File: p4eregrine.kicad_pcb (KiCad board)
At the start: 6 copper layers, 39.5 x 39.5 mm, 359 parts, among them J5 Conn_Coaxial, Q10 NMOS, Q11 NMOS, Q12 NMOS, Q13 NMOS, Q14 NMOS, Q15 NMOS, Q16 NMOS, Q17 NMOS, Q18 NMOS, Q19 NMOS, Q20 NMOS, Q21 NMOS, Q22 NMOS, Q23 NMOS, Q24 NMOS, Q25 NMOS, Q26 NMOS, Q27 NMOS, Q28 NMOS, Q5 NMOS, Q6 NMOS, Q7 NMOS, Q8 NMOS, Q9 NMOS, U1 ESP32-P4NRW32X, U10 FPC-1.0FX-15PWCR-H20, U11 VL53L1CXV0FY1, U12 LIS2MDL, U13 LSM6DS3, U14 PMW3901MB-TXQT_C43496881, U15 TPD2EUSB30A, U16 DRV8328ARUYR, U17 TPS62933, U19 DRV8328ARUYR, U2 LPS22HB, U20 STM32G071GBU6, U22 DRV8328ARUYR, U23 STM32G071GBU6, U25 DRV8328ARUYR, U26 STM32G071GBU6, U3 W25Q128JVP, U30 STM32G071GBU6, U4 ESP32-C5HF4, U5 LFD182G45DCHD277, U6 TLV62569DBV, U7 GT-USB-7079C, U8 INA190A2IDCKR, U9 TPS2121RUXR, Y1 Crystal_GND24, Y2 Crystal_GND24

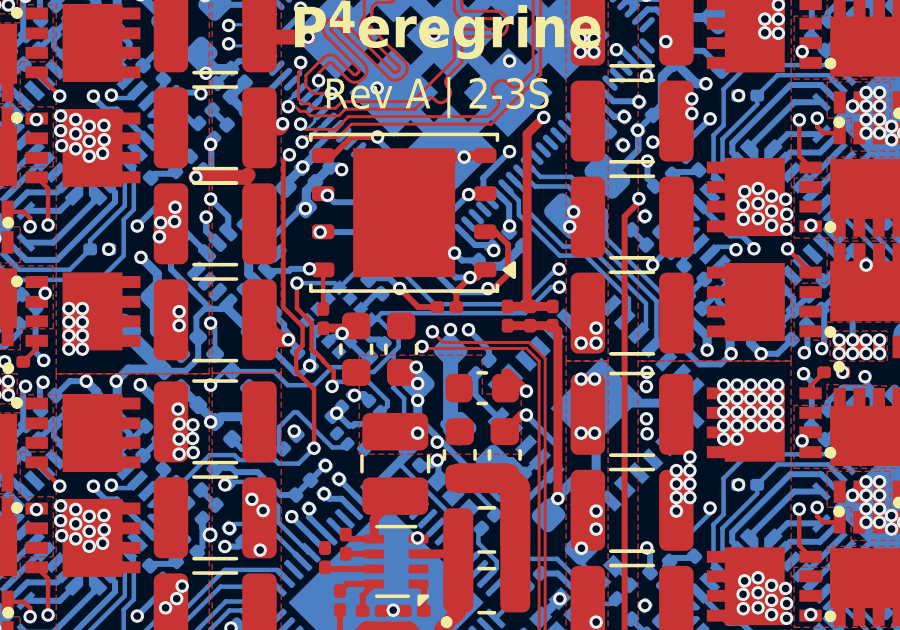
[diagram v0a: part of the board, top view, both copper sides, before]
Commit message: Add power supply comments to schematic
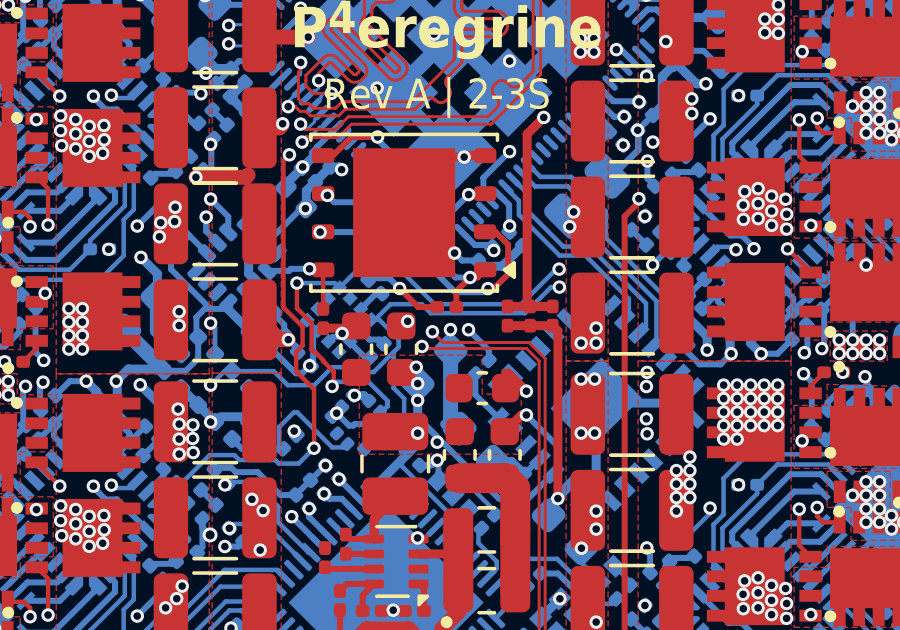
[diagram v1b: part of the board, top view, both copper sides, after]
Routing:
- net GND: vias 257 -> 258
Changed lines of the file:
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@@
 	)
 	(via
+		(at 149.512973 88.370643)
+		(size 0.45)
+		(drill 0.25)
+		(layers "F.Cu" "B.Cu")
+		(remove_unused_layers yes)
+		(keep_end_layers yes)
+		(free yes)
+		(zone_layer_connections "In1.Cu" "In4.Cu")
+		(net "GND")
+	)
+	(via
 		(at 145.535377 88.982263)
 		(size 0.45)
@@
 	)
 	(segment
+		(start 150.282378 88.1)
+		(end 149.982378 87.8)
+		(width 0.15)
+		(layer "B.Cu")
+		(net "I2C_SDA")
+	)
+	(segment
 		(start 145.046825 90.030702)
 		(end 145.516123 90.5)
@@
 	)
 	(segment
+		(start 154.571253 87.230505)
+		(end 154.293759 87.230505)
+		(width 0.15)
+		(layer "B.Cu")
+		(net "I2C_SDA")
+	)
+	(segment
 		(start 157.204961 81.035675)
 		(end 157.22458 81.055295)
@@
 	)
 	(segment
-		(start 147 89.9)
-		(end 147.953848 89.9)
+		(start 148.941206 87.8)
+		(end 148.425303 88.315903)
 		(width 0.15)
 		(layer "B.Cu")
@@
 	)
 	(segment
-		(start 153.424264 88.1)
-		(end 148.641206 88.1)
+		(start 147 89.9)
+		(end 147.953848 89.9)
 		(width 0.15)
 		(layer "B.Cu")
@@
 	)
 	(segment
-		(start 154.293759 87.230505)
-		(end 153.424264 88.1)
+		(start 148.560682 92.435816)
+		(end 149.056824 92.435816)
 		(width 0.15)
 		(layer "B.Cu")
@@
 	)
 	(segment
-		(start 148.560682 92.435816)
-		(end 149.056824 92.435816)
+		(start 148.425303 88.315903)
+		(end 148.301788 88.315903)
 		(width 0.15)
 		(layer "B.Cu")
@@
 	)
 	(segment
-		(start 154.571253 87.230505)
-		(end 154.293759 87.230505)
-		(width 0.15)
-		(layer "B.Cu")
-		(net "I2C_SDA")
-	)
-	(segment
 		(start 149.046253 89.397429)
 		(end 149.212121 89.231561)
@@
 	)
 	(segment
-		(start 148.425303 88.315903)
-		(end 148.301788 88.315903)
+		(start 159.426411 72.357909)
+		(end 159.396302 72.388018)
 		(width 0.15)
 		(layer "B.Cu")
@@
 	)
 	(segment
-		(start 159.426411 72.357909)
-		(end 159.396302 72.388018)
+		(start 154.293759 87.230505)
+		(end 153.424264 88.1)
 		(width 0.15)
 		(layer "B.Cu")
@@
 	)
 	(segment
-		(start 148.641206 88.1)
-		(end 148.425303 88.315903)
-		(width 0.15)
-		(layer "B.Cu")
-		(net "I2C_SDA")
-	)
-	(segment
 		(start 156.371251 81.035675)
 		(end 157.204961 81.035675)
@@
 	)
 	(segment
+		(start 153.424264 88.1)
+		(end 150.282378 88.1)
+		(width 0.15)
+		(layer "B.Cu")
+		(net "I2C_SDA")
+	)
+	(segment
 		(start 147.953848 89.9)
 		(end 148.116103 90.062255)
@@
 		(width 0.15)
 		(layer "B.Cu")
+		(net "I2C_SDA")
+	)
+	(segment
+		(start 149.982378 87.8)
+		(end 148.941206 87.8)
+		(width 0.15)
+		(layer "B.Cu")

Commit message: Add BAT_ISENSE filtering cap and improve 3v3 plane continuity
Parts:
- added C62: 100n, Capacitor_SMD:C_0201_0603Metric, B.Cu at (156.7, 84.6)
- C67: value 22u -> 10u
- moved C1 0.22 mm to (155.3, 84.1)
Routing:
- net +3V3: track 137.0 -> 140.2 mm, vias 48 -> 47
- net GND: track 234.7 -> 236.4 mm, vias 258 -> 256
- net BAT_ISENSE: track 33.9 -> 32.7 mm
- net DSHOT_2: track 23.3 -> 24.0 mm, vias 2 -> 3
